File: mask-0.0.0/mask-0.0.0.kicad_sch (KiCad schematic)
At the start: 73 parts, among them SW1 SW_Push, SW10 SW_Push, SW11 SW_Push, SW12 SW_Push, SW13 SW_Push, SW13_1 SW_Push, SW14 SW_Push, SW15 SW_Push, SW16 SW_Push, SW17 SW_Push, SW18 SW_Push, SW19 SW_Push, SW2 SW_Push, SW20 SW_Push, SW20_1 SW_Push, SW21 SW_Push, SW22 SW_Push, SW23 SW_Push, SW24 SW_Push, SW25 SW_Push, SW26 SW_Push, SW27 SW_Push, SW27_1 SW_Push, SW28 SW_Push, SW29 SW_Push, SW3 SW_Push, SW30 SW_Push, SW31 SW_Push, SW32 SW_Push, SW33 SW_Push, SW34 SW_Push, SW35 SW_Push, SW4 SW_Push, SW5 SW_Push, SW6 SW_Push, SW7 SW_Push, SW8 SW_Push, SW9 SW_Push

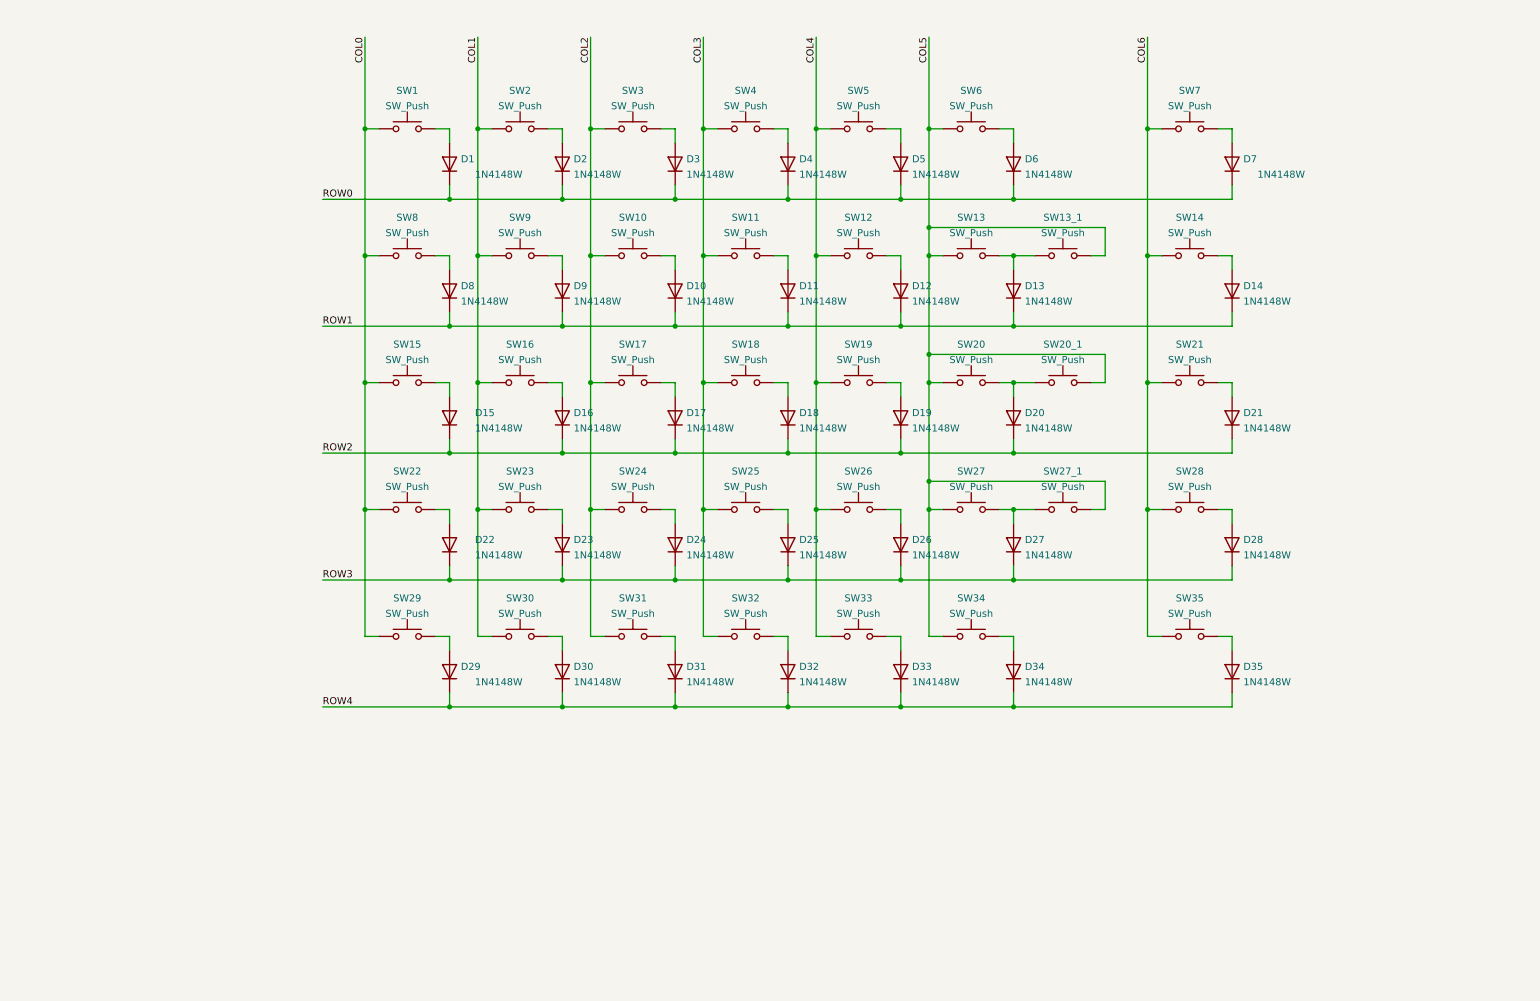
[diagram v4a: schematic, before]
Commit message: 0.0.0: create symbol/footprint for ble module, some schematic progress
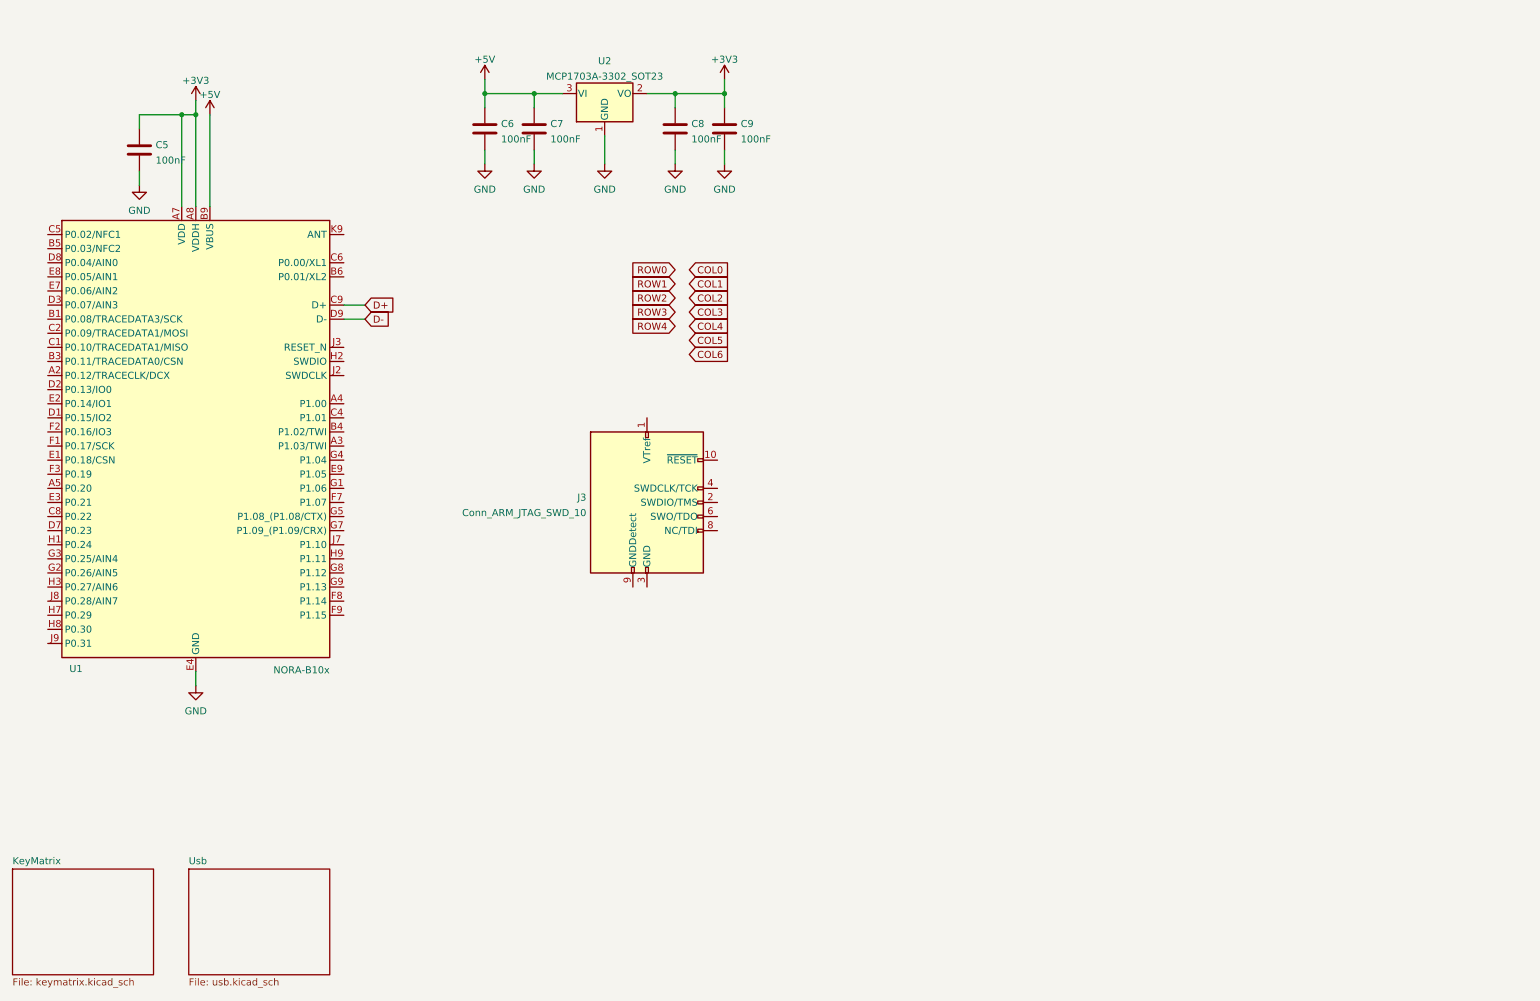
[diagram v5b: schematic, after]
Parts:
- removed D1, D10, D11, D12, D13, D14, D15, D16, D17, D18, D19, D2, D20, D21, D22, D23, D24, D25, D26, D27, D28, D29, D3, D30, D31, D32, D33, D34, D35, D4, D5, D6, D7, D8, D9: 1N4148W, Diode_SMD_TopBottom:D_SOD-123_TopBottom, symbol Diode:1N4148W
- removed SW1, SW10, SW11, SW12, SW13, SW14, SW15, SW16, SW17, SW18, SW19, SW2, SW20, SW21, SW22, SW23, SW24, SW25, SW26, SW27, SW28, SW29, SW3, SW30, SW32, SW33, SW34, SW35, SW4, SW5, SW6, SW7, SW8, SW9: SW_Push, Button_Switch_Keyboard_Swappable:SW_Cherry_MX_1.00u_Kailh_Socket_TopBottom, symbol Switch:SW_Push
- removed SW13_1, SW20_1, SW27_1: SW_Push, Button_Switch_Keyboard_Swappable:SW_Cherry_MX_2.00u_Kailh_Socket_NoStabilizer_TopBottom, symbol Switch:SW_Push
- removed SW31: SW_Push, Button_Switch_Keyboard_Swappable:SW_Cherry_MX_1.25u_Kailh_Socket_TopBottom, symbol Switch:SW_Push
- added C5, C6, C7, C8, C9: 100nF, Capacitor_SMD:C_0603_1608Metric, symbol Device:C
- added J3: Conn_ARM_JTAG_SWD_10, Connector_PinHeader_1.27mm:PinHeader_2x05_P1.27mm_Vertical_SMD, symbol Connector:Conn_ARM_JTAG_SWD_10
- added U1: NORA-B10x, RF_Module_User:Ublox_NORA-B10x, symbol RF_Module_User:NORA-B10x
- added U2: MCP1703A-3302_SOT23, Package_TO_SOT_SMD:SOT-23, symbol Regulator_Linear:MCP1703A-3302_SOT23
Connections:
- new net: J3.3 (GND), J3.5 (GND)
- new net +3V3: C5.1, C8.1, C9.1, U1.A7 (VDD), U1.A8 (VDDH), U1.B7 (VDD), U2.2 (VO)
- new net +5V: C6.1, C7.1, U1.B9 (VBUS), U2.3 (VI)
- new net D+: U1.C9 (D+)
- new net D-: U1.D9 (D-)
- new net GND: C5.2, C6.2, C7.2, C8.2, C9.2, U1.A1 (GND), U1.A9 (GND), U1.B2 (GND), U1.B8 (GND), U1.E4 (GND), U1.E5 (GND), U1.F4 (GND), U1.F5 (GND), U1.K2 (GND), U1.K3 (GND), U1.K5 (GND), U1.K7 (GND), U1.K8 (GND), U1.L1 (GND), U1.L9 (GND), U1.M1 (GND), U1.M2 (GND), U1.M8 (GND), U1.M9 (GND), U2.1 (GND)
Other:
- added sheet KeyMatrix (keymatrix.kicad_sch)
- added sheet Usb (usb.kicad_sch)

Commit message: schematic: connect debugger
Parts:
- added C?: 100nF, Capacitor_SMD:C_0603_1608Metric, symbol Device:C
- added R?: 10k, Resistor_SMD:R_0603_1608Metric, symbol Device:R
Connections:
- net +3V3: now also J3.1 (VTref), R?.1
- net GND: now also J3.3 (GND), J3.5 (GND), J3.9 (GNDDetect), C?.2
- net RESET: now reaches J3.10 (~{RESET})
- net RESET: now also U1.J3 (RESET_N), C?.1, R?.2
- net SWDIO: now reaches J3.2 (SWDIO/TMS)
- net SWDIO: now also U1.H2 (SWDIO)
- net SWDCLK: now reaches J3.4 (SWDCLK/TCK)
- net SWDCLK: now also U1.J2 (SWDCLK)
- net SWO: now reaches J3.6 (SWO/TDO)
- net SWO: now also U1.B3 (P0.11/TRACEDATA0/CSN)
- no-connect marks 0 -> 1
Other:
- moved on the sheet: C5, U1

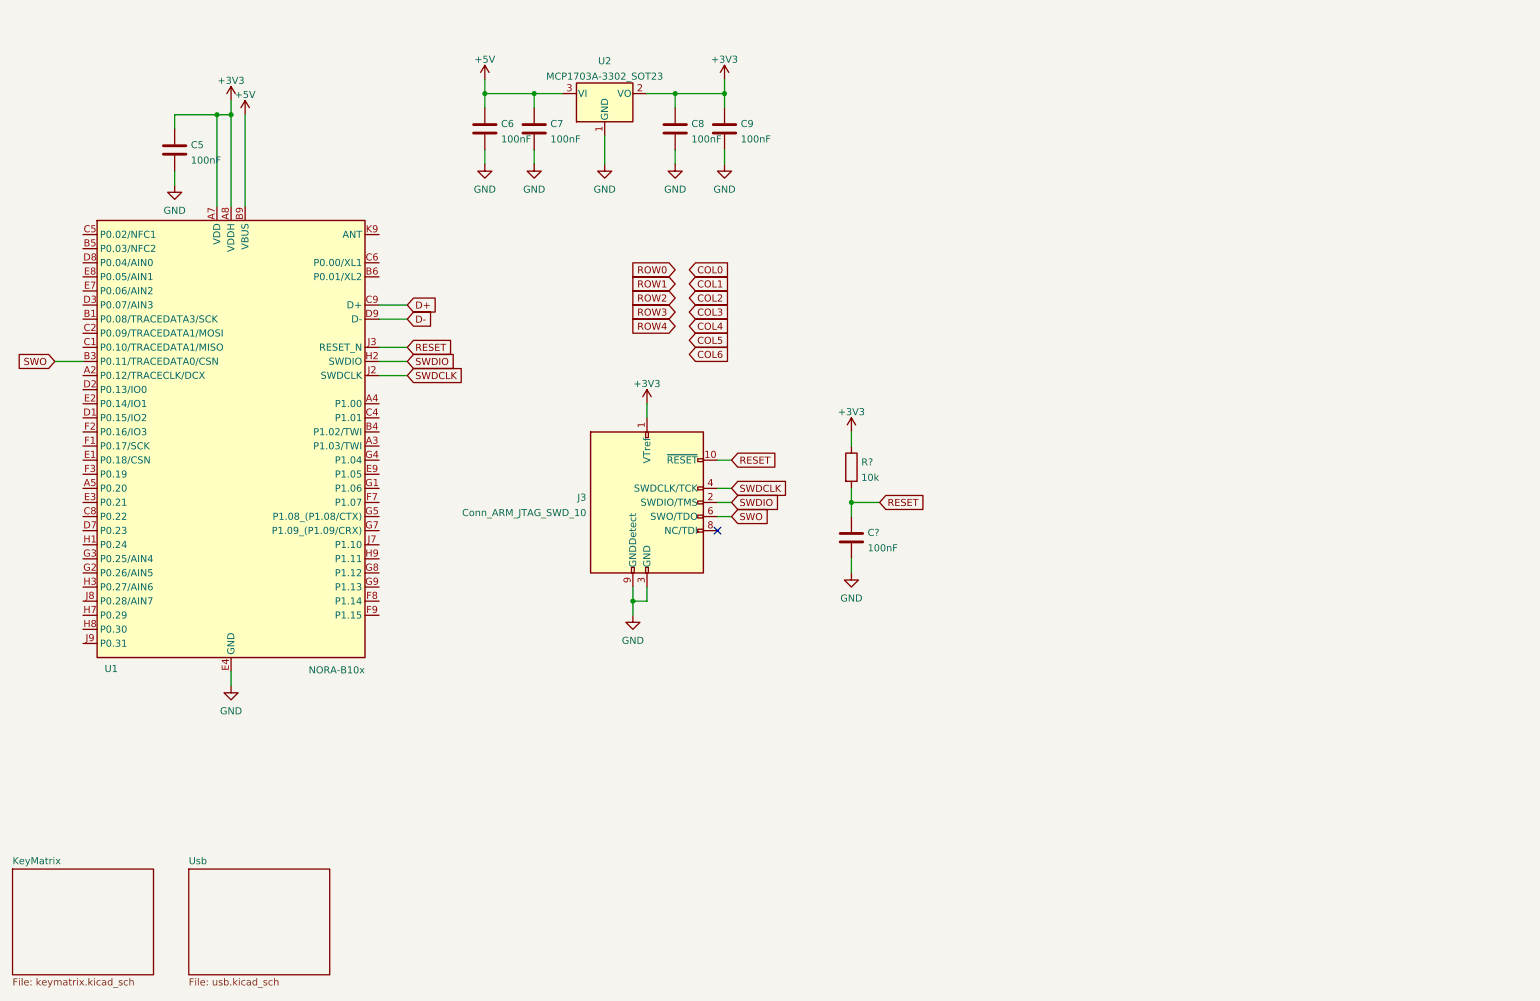
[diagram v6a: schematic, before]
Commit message: add leds (sk2812) and level converter
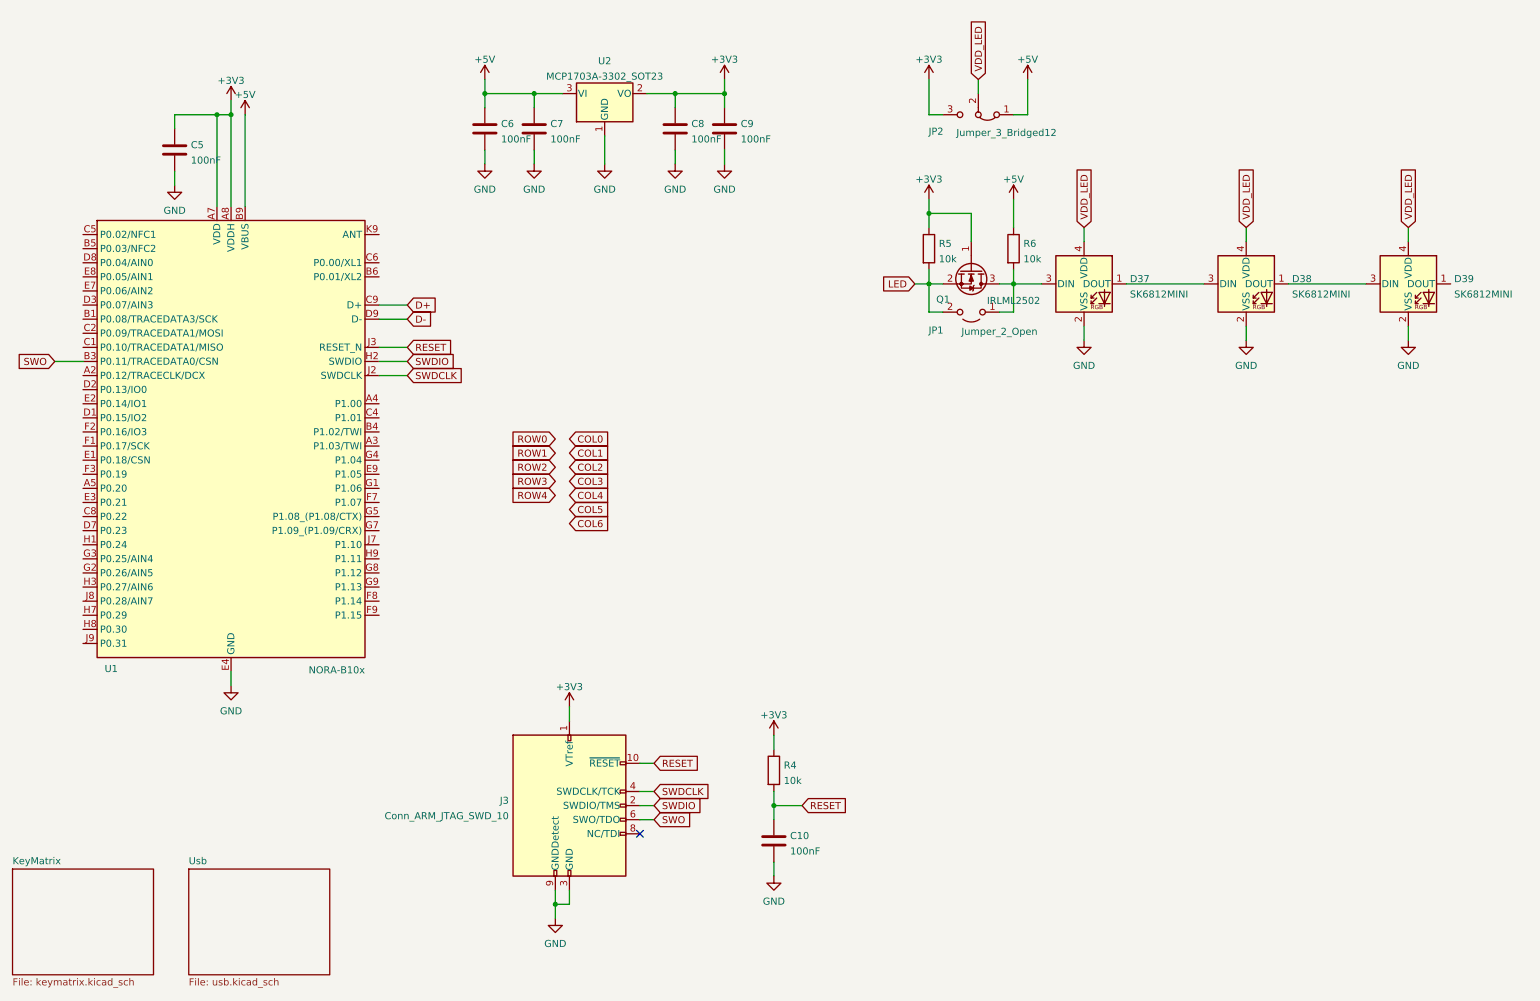
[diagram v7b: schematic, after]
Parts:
- added D37, D38, D39: SK6812MINI, LED_SMD:LED_SK6812MINI_PLCC4_3.5x3.5mm_P1.75mm, symbol LED:SK6812MINI
- added JP1: Jumper_2_Open, Jumper:SolderJumper-2_P1.3mm_Open_RoundedPad1.0x1.5mm, symbol Jumper:Jumper_2_Open
- added JP2: Jumper_3_Bridged12, Jumper:SolderJumper-3_P1.3mm_Bridged12_RoundedPad1.0x1.5mm, symbol Jumper:Jumper_3_Bridged12
- added Q1: IRLML2502, Package_TO_SOT_SMD:SOT-23, symbol Device:Q_NMOS_GSD
- added R5, R6: 10k, Resistor_SMD:R_0603_1608Metric, symbol Device:R
- gave numbers to parts that had none: 2
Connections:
- net +3V3: now also JP2.3 (B), Q1.1 (G), R5.1
- net +5V: now also JP2.1 (A), R6.1
- net GND: now also D37.2 (VSS), D38.2 (VSS), D39.2 (VSS)
- new net: D38.1 (DOUT), D39.3 (DIN)
- new net: D37.1 (DOUT), D38.3 (DIN)
- new net: D37.3 (DIN), JP1.1 (A), Q1.3 (D), R6.2
- new net LED: JP1.2 (B), Q1.2 (S), R5.2
- new net VDD_LED: D37.4 (VDD), D38.4 (VDD), D39.4 (VDD), JP2.2 (C)
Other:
- moved on the sheet: C10, J3, R4

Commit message: udpate routing
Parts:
- removed C7, C8: 100nF, Capacitor_SMD:C_0603_1608Metric, symbol Device:C
- added D2, D4, D6: SK6812MINI, LED_SMD:LED_SK6812MINI_PLCC4_3.5x3.5mm_P1.75mm, symbol LED:SK6812MINI
- added J1: Conn_02x05_Counter_Clockwise, Connector:Tag-Connect_TC2050-IDC-NL_2x05_P1.27mm_Vertical, symbol Connector_Generic:Conn_02x05_Counter_Clockwise
- renumbered C5 to C1, C6 to C2, C9 to C3, C10 to C4, D37 to D1, D38 to D3, D39 to D5, J3 to J2, R4 to R1, R5 to R2, R6 to R3
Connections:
- net +3V3: now also J1.1 (Pin_1), J1.5 (Pin_5)
- net GND: now also D2.2 (VSS), D4.2 (VSS), D6.2 (VSS), J1.3 (Pin_3); no longer J2.9 (GNDDetect)
- net RESET: now also J1.10 (Pin_10)
- net SWDCLK: now also J1.4 (Pin_4)
- net SWDIO: now also J1.2 (Pin_2)
- net SWO: now also J1.6 (Pin_6)
- net VDD_LED: now also D2.4 (VDD), D4.4 (VDD), D6.4 (VDD)
- net at D3.1 (DOUT), D5.3 (DIN): now also D4.1 (DOUT), D6.3 (DIN)
- net at D1.1 (DOUT), D3.3 (DIN): now also D2.1 (DOUT), D4.3 (DIN)
- net at D1.3 (DIN), JP1.1 (A), Q1.3 (D)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: now also D2.3 (DIN)
- net at D5.1 (DOUT): now also D6.1 (DOUT)
- no-connect marks 1 -> 5
